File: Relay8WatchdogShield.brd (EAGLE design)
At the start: 53.3 x 53.3 mm, 9 parts, among them J1 Digital_0_7, J2 Analog, J3 Digital_8_13, J4 Analog

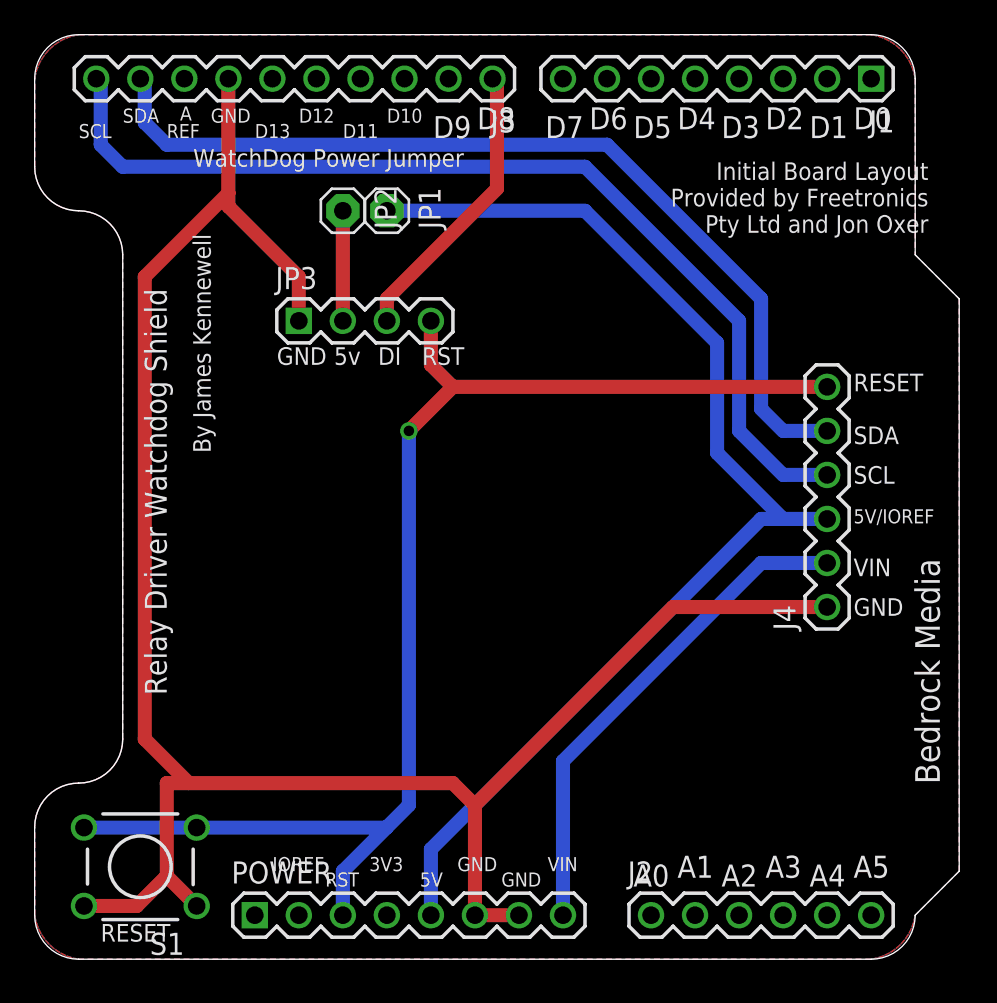
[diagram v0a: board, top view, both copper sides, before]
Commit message: Updated I2c Header
Changed Header from 1x6 to 2x3 IDC Shrouded Header.
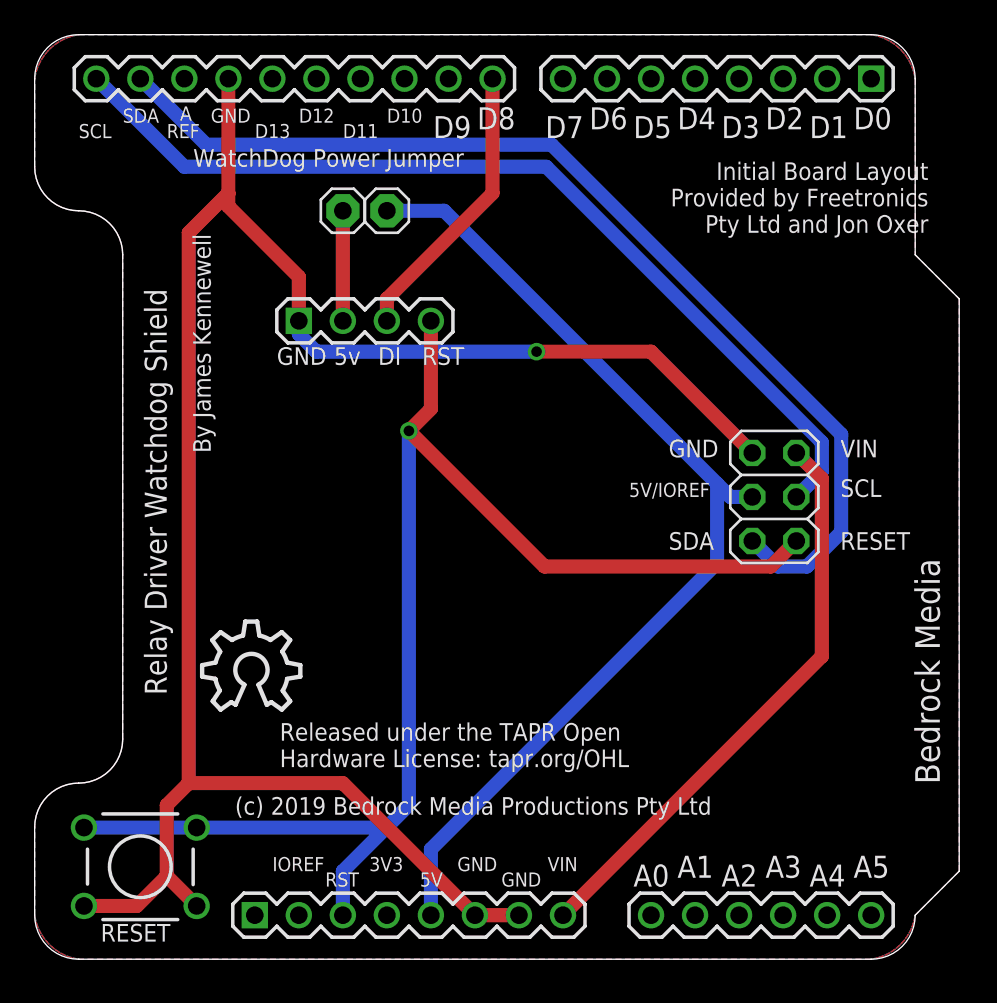
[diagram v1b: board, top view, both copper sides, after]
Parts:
- removed J4: Analog, freetronics:1X06
- added JP4: (no value), pinhead:2X03
- added U$1: (no value), OSHW:OSHW_10X200_NOTEXT
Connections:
- net 5V: now also JP4.4; no longer J4.3
- net GND: now also JP4.6; no longer J4.1
- net RESET: now also JP4.1; no longer J4.6
- net SCL: now also JP4.3; no longer J4.4
- net SDA: now also JP4.2; no longer J4.5
- net VIN: now also JP4.5; no longer J4.2
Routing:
- net 5V: track 68.5 -> 59.7 mm
- net SDA: track 53.1 -> 61.1 mm
- net VIN: track 28.9 -> 33.5 mm
- net RESET: track 76.5 -> 80.0 mm
- net SCL: track 57.4 -> 54.3 mm
- net GND: track 118.3 -> 116.4 mm, vias 0 -> 1
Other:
- board text added: "(c) 2019 Bedrock Media Productions Pty Ltd"
- board text added: "Released under the TAPR Open Hardware License: tapr.org/OHL"
